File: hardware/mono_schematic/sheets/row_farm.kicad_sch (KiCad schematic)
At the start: 98 parts

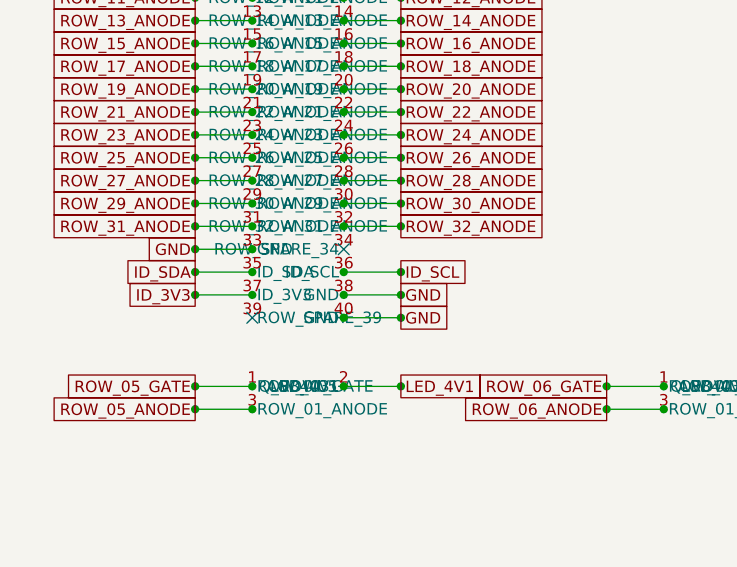
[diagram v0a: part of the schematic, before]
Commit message: mono_electronics v14: installation-build headers J_RH1/J_CH1 (2x20 1.27mm SMD, pin n = FFC pin n) + 64 PESD5V0S1BL, DNP in wearable; board 160.5x99.5; wearable/installation BOM+CPL; gates clean (DRC 0/0/0, ERC 0, 0 diffs, прозвонка 309/309); fab v14
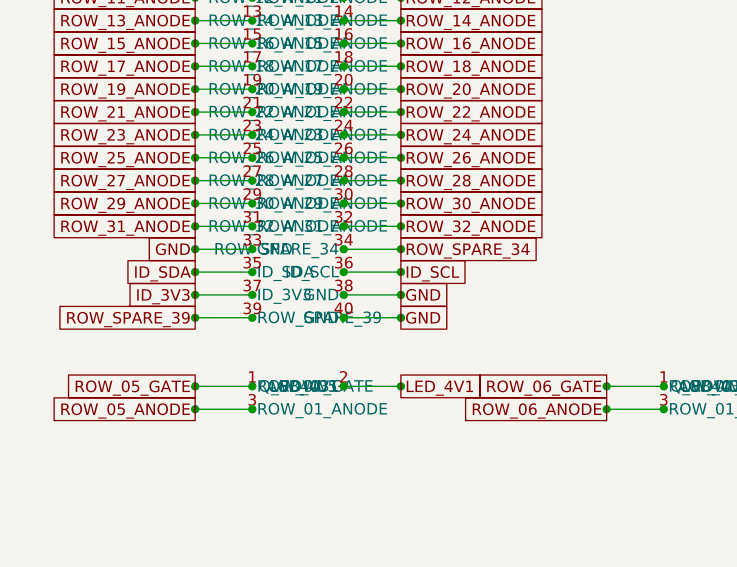
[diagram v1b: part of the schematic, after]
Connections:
- net ROW_SPARE_34: now reaches J_ROW1.34 (ROW_SPARE_34)
- net ROW_SPARE_39: now reaches J_ROW1.39 (ROW_SPARE_39)
- no-connect marks 2 -> 0
